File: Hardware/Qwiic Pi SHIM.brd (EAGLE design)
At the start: 10.2 x 14 mm, 13 parts, among them J1 Qwiic Right Angle, U2 3.3V/600mA

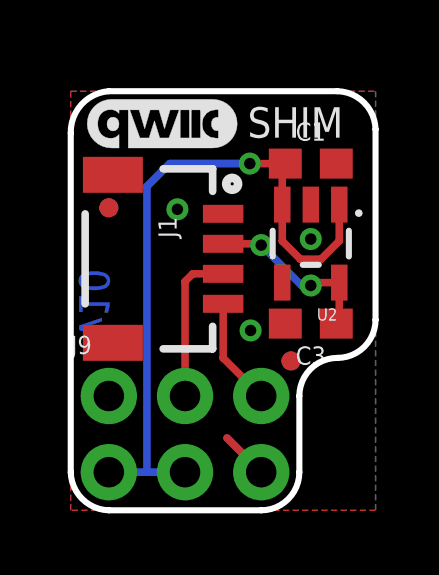
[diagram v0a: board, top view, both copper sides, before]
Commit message: fixed orientation so it goes over the pi
added ordering instructions - 0.8mm thickness
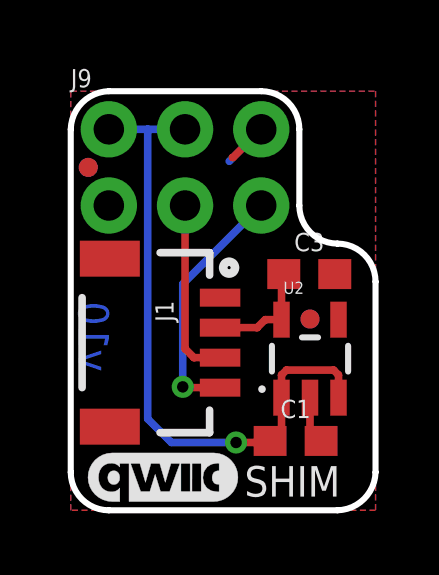
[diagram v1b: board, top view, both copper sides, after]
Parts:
- added U$4: SPECIAL_INSTRUCTIONS-ORDERING, SparkFun-Aesthetics:ORDERING_INSTRUCTIONS
- moved U$3 11.8 mm to (3.05, 1.12)
- moved LOGO1 10.6 mm to (1.83, 1.68)
- moved FRAME1 10.5 mm to (-11.4, -14.0)
- moved U$1 9.96 mm to (9.42, 0.36)
- moved C1 9.26 mm to (7.49, 2.31)
- moved J9 8.89 mm to (3.81, 11.4)
- moved U2 3.84 mm to (7.98, 5.05), turned to 0 degrees
- moved J1 2.80 mm to (4.98, 5.59)
- moved C3 1.65 mm to (7.95, 7.87), turned to 0 degrees
- moved FD2 1.53 mm to (7.98, 6.38)
- moved FD3 1.53 mm to (7.98, 6.38)
- moved FD1 1.51 mm to (0.58, 11.4)
- moved FD4 1.51 mm to (0.58, 11.4)
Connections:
- net 5V: now also J9.2, J9.4; no longer J9.1, J9.3
- net GND: now also J9.6; no longer J9.5
- net NC: now also J9.1; no longer J9.2
- net SCL: now also J9.5; no longer J9.6
- net SDA: now also J9.3; no longer J9.4
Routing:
- net SCL: track 3.60 -> 8.38 mm, vias 0 -> 1
- net 3.3V: track 5.89 -> 3.71 mm, vias 2 -> 0
- net 5V: track 23.2 -> 21.8 mm
- net GND: track 3.23 -> 4.46 mm, vias 3 -> 0
- net SDA: track 5.19 -> 6.07 mm
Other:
- outline, holes or cut-outs redrawn
- board text added: "0.8MM Thickness"

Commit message: Single slot version done
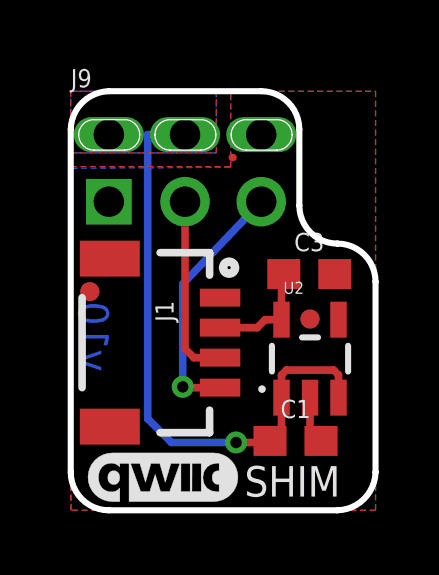
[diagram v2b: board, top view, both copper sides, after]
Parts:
- J9: device SparkFun-Connectors:2X3-NS -> Qwiic Pi SHIM:SPARKFUN-CONNECTORS_2X3-NS_PISHIM_LOCKING_SLOTS
- moved FD1 4.14 mm to (0.64, 7.29)
- moved FD4 4.14 mm to (0.64, 7.29)
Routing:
- net GND: track 4.46 -> 1.62 mm
- net 5V: track 21.8 -> 20.3 mm
- added copper zone on layer 1, net 5V
- added copper zone on layer 16, net 5V
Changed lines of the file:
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@@
 <layer number="27" name="tValues" color="7" fill="1" visible="no" active="yes"/>
 <layer number="28" name="bValues" color="7" fill="1" visible="no" active="yes"/>
-<layer number="29" name="tStop" color="7" fill="3" visible="no" active="yes"/>
-<layer number="30" name="bStop" color="7" fill="6" visible="no" active="yes"/>
+<layer number="29" name="tStop" color="7" fill="3" visible="yes" active="yes"/>
+<layer number="30" name="bStop" color="7" fill="6" visible="yes" active="yes"/>
 <layer number="31" name="tCream" color="7" fill="4" visible="no" active="yes"/>
 <layer number="32" name="bCream" color="7" fill="5" visible="no" active="yes"/>
@@
 <layer number="44" name="Drills" color="7" fill="1" visible="no" active="yes"/>
 <layer number="45" name="Holes" color="7" fill="1" visible="yes" active="yes"/>
-<layer number="46" name="Milling" color="3" fill="1" visible="no" active="yes"/>
+<layer number="46" name="Milling" color="3" fill="1" visible="yes" active="yes"/>
 <layer number="47" name="Measures" color="7" fill="1" visible="yes" active="yes"/>
 <layer number="48" name="Document" color="7" fill="1" visible="no" active="yes"/>
@@
 </class>
 </classes>
-<designrules name="SparkFun-2-layer-TIGHT">
+<designrules name="SparkFun-2-layer-TIGHT *">
 <description language="en">&lt;b&gt;SparkFun 2 Layer Design Rule Checks - STANDARD/TIGHT/FAB-LIMIT&lt;/b&gt;
 &lt;p&gt;
@@
 <param name="msMicroVia" value="9.99mm"/>
 <param name="msBlindViaRatio" value="0.5"/>
-<param name="rvPadTop" value="0.25"/>
-<param name="rvPadInner" value="0.25"/>
-<param name="rvPadBottom" value="0.25"/>
+<param name="rvPadTop" value="0.05"/>
+<param name="rvPadInner" value="0.05"/>
+<param name="rvPadBottom" value="0.05"/>
 <param name="rvViaOuter" value="0.25"/>
 <param name="rvViaInner" value="0.25"/>
 <param name="rvMicroViaOuter" value="0.25"/>
 <param name="rvMicroViaInner" value="0.25"/>
-<param name="rlMinPadTop" value="7mil"/>
+<param name="rlMinPadTop" value="2mil"/>
 <param name="rlMaxPadTop" value="20mil"/>
-<param name="rlMinPadInner" value="7mil"/>
+<param name="rlMinPadInner" value="2mil"/>
 <param name="rlMaxPadInner" value="20mil"/>
-<param name="rlMinPadBottom" value="7mil"/>
+<param name="rlMinPadBottom" value="2mil"/>
 <param name="rlMaxPadBottom" value="20mil"/>
 <param name="rlMinViaOuter" value="7mil"/>
@@
 <param name="checkWireStubs" value="1"/>
 <param name="checkPolygonWidth" value="0"/>
-<param name="useDiameter" value="13"/>
+<param name="useDiameter" value="15"/>
 <param name="maxErrors" value="50"/>
 </designrules>
@@
 <element name="FRAME1" library="SparkFun-Aesthetics" package="CREATIVE_COMMONS" value="FRAME-LETTER" x="-11.43" y="-13.97" smashed="yes"/>
 <element name="LOGO1" library="SparkFun-Aesthetics" package="OSHW-LOGO-MINI" value="OSHW-LOGOMINI" x="1.8288" y="1.6764" smashed="yes" rot="MR0"/>
-<element name="FD1" library="SparkFun-Aesthetics" package="FIDUCIAL-MICRO" value="FIDUCIALUFIDUCIAL" x="0.5842" y="11.43" smashed="yes" rot="R180"/>
+<element name="FD1" library="SparkFun-Aesthetics" package="FIDUCIAL-MICRO" value="FIDUCIALUFIDUCIAL" x="0.635" y="7.2898" smashed="yes" rot="R180"/>
 <element name="FD2" library="SparkFun-Aesthetics" package="FIDUCIAL-MICRO" value="FIDUCIALUFIDUCIAL" x="7.9756" y="6.3754" smashed="yes" rot="R180"/>
 <element name="J1" library="SparkFun-Connectors" package="1X04_1MM_RA" value="Qwiic Right Angle" x="4.9784" y="5.588" smashed="yes" rot="R270">
@@
 </element>
 <element name="FD3" library="SparkFun-Aesthetics" package="FIDUCIAL-MICRO" value="FIDUCIALUFIDUCIAL" x="7.9756" y="6.3754" smashed="yes" rot="MR0"/>
-<element name="FD4" library="SparkFun-Aesthetics" package="FIDUCIAL-MICRO" value="FIDUCIALUFIDUCIAL" x="0.5842" y="11.43" smashed="yes" rot="MR0"/>
-<element name="J9" library="SparkFun-Connectors" package="2X3-NS" value="" x="3.81" y="11.43" smashed="yes">
+<element name="FD4" library="SparkFun-Aesthetics" package="FIDUCIAL-MICRO" value="FIDUCIALUFIDUCIAL" x="0.635" y="7.2898" smashed="yes" rot="MR0"/>
+<element name="J9" library="Qwiic Pi SHIM" package="SPARKFUN-CONNECTORS_2X3-NS_PISHIM_LOCKING_SLOTS" value="" x="3.81" y="11.43" smashed="yes">
 <attribute name="NAME" x="0" y="14.097" size="0.6096" layer="25" font="vector" ratio="20"/>
 <attribute name="VALUE" x="0" y="7.493" size="0.6096" layer="27" font="vector" ratio="20"/>
@@
 <signal name="GND" class="1">
 <polygon width="0.254" layer="1">
-<vertex x="0" y="13.97"/>
+<vertex x="0" y="11.4554"/>
+<vertex x="5.334" y="11.4554"/>
+<vertex x="5.334" y="13.97"/>
 <vertex x="10.16" y="13.97"/>
 <vertex x="10.16" y="0"/>
@@
 </polygon>
 <polygon width="0.254" layer="16">
-<vertex x="0" y="13.97"/>
+<vertex x="0.0254" y="11.39913125"/>
+<vertex x="4.8006" y="11.43"/>
+<vertex x="5.334" y="11.43"/>
+<vertex x="5.334" y="13.97"/>
 <vertex x="10.16" y="13.97"/>
 <vertex x="10.16" y="0"/>
-<vertex x="0" y="0"/>
+<vertex x="0.0254" y="0"/>
 </polygon>
 <contactref element="J1" pad="1"/>
@@
 <contactref element="U2" pad="2"/>
 <contactref element="J9" pad="6"/>
-<wire x1="6.35" y1="12.7" x2="5.2832" y2="11.6332" width="0.254" layer="16"/>
-<wire x1="6.35" y1="12.7" x2="5.4102" y2="11.7602" width="0.254" layer="1"/>
 <wire x1="5.4102" y1="11.7602" x2="5.3848" y2="11.7602" width="0.254" layer="1"/>
 <wire x1="7.9756" y1="3.7545" x2="7.9756" y2="2.6788" width="0.254" layer="1"/>
@@
 <contactref element="J1" pad="3"/>
 <contactref element="J9" pad="3"/>
-<wire x1="3.81" y1="5.3848" x2="3.81" y2="10.16" width="0.254" layer="1"/>
+<wire x1="3.81" y1="5.3848" x2="3.81" y2="10.287" width="0.254" layer="1"/>
 <wire x1="4.9784" y1="5.088" x2="4.1068" y2="5.088" width="0.254" layer="1"/>
 <wire x1="4.1068" y1="5.088" x2="3.81" y2="5.3848" width="0.254" layer="1"/>
@@
 <contactref element="J1" pad="4"/>
 <contactref element="J9" pad="5"/>
-<wire x1="6.35" y1="10.16" x2="3.7338" y2="7.5438" width="0.254" layer="16"/>
+<wire x1="6.35" y1="10.287" x2="3.7338" y2="7.5438" width="0.254" layer="16"/>
 <wire x1="3.7338" y1="7.5438" x2="3.7338" y2="4.1148" width="0.254" layer="16"/>
 <via x="3.7338" y="4.1148" extent="1-16" drill="0.381"/>
@@
 <contactref element="J9" pad="4"/>
 <contactref element="J9" pad="2"/>
-<wire x1="3.81" y1="12.7" x2="2.5654" y2="12.7" width="0.254" layer="16"/>
-<wire x1="2.5654" y1="12.7" x2="1.27" y2="12.7" width="0.254" layer="16"/>
-<wire x1="2.5654" y1="12.7" x2="2.5654" y2="3.048" width="0.254" layer="16"/>
 <wire x1="7.0256" y1="3.7545" x2="7.0256" y2="2.694" width="0.254" layer="1"/>
 <wire x1="7.0256" y1="2.694" x2="6.643" y2="2.3114" width="0.254" layer="1"/>
@@
 <wire x1="3.3528" y1="2.2606" x2="5.5118" y2="2.2606" width="0.254" layer="16"/>
 <via x="5.5118" y="2.2606" extent="1-16" drill="0.381"/>
-<wire x1="2.5654" y1="3.048" x2="3.3528" y2="2.2606" width="0.254" layer="16"/>
+<wire x1="3.3528" y1="2.2606" x2="2.5654" y2="3.048" width="0.254" layer="16"/>
 <wire x1="6.643" y1="2.3114" x2="6.5922" y2="2.2606" width="0.254" layer="1"/>
 <wire x1="6.5922" y1="2.2606" x2="5.5118" y2="2.2606" width="0.254" layer="1"/>
+<polygon width="0.2032" layer="1">
+<vertex x="4.8514" y="13.97"/>
+<vertex x="0" y="13.97"/>
+<vertex x="0" y="11.9126"/>
+<vertex x="4.8514" y="11.9126"/>
+</polygon>
+<wire x1="2.5654" y1="12.5222" x2="3.81" y2="12.5222" width="0.254" layer="16"/>
+<wire x1="2.5654" y1="3.048" x2="2.5654" y2="12.5222" width="0.254" layer="16"/>
+<polygon width="0.2032" layer="16">
+<vertex x="4.8514" y="11.9126"/>
+<vertex x="0" y="11.9126"/>
+<vertex x="0" y="13.97"/>
+<vertex x="4.8514" y="13.97"/>
+</polygon>
 </signal>
 <signal name="NC">
